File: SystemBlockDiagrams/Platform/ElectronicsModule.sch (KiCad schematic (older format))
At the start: 3 parts

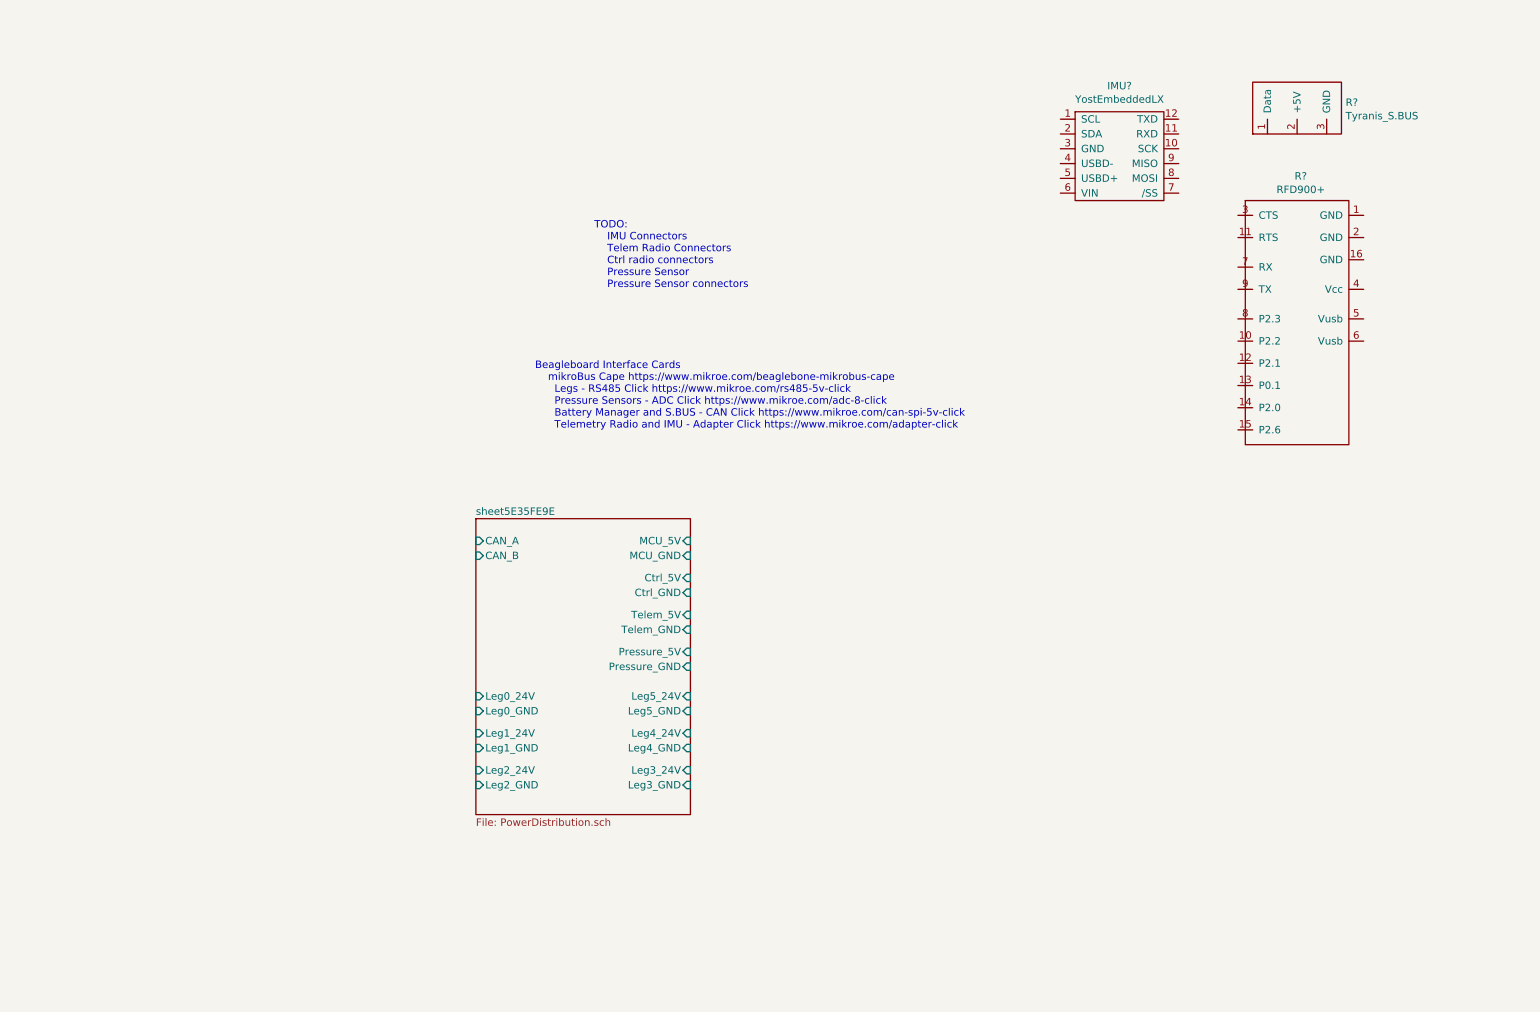
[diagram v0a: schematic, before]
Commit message: Update part numbers for BOM generation
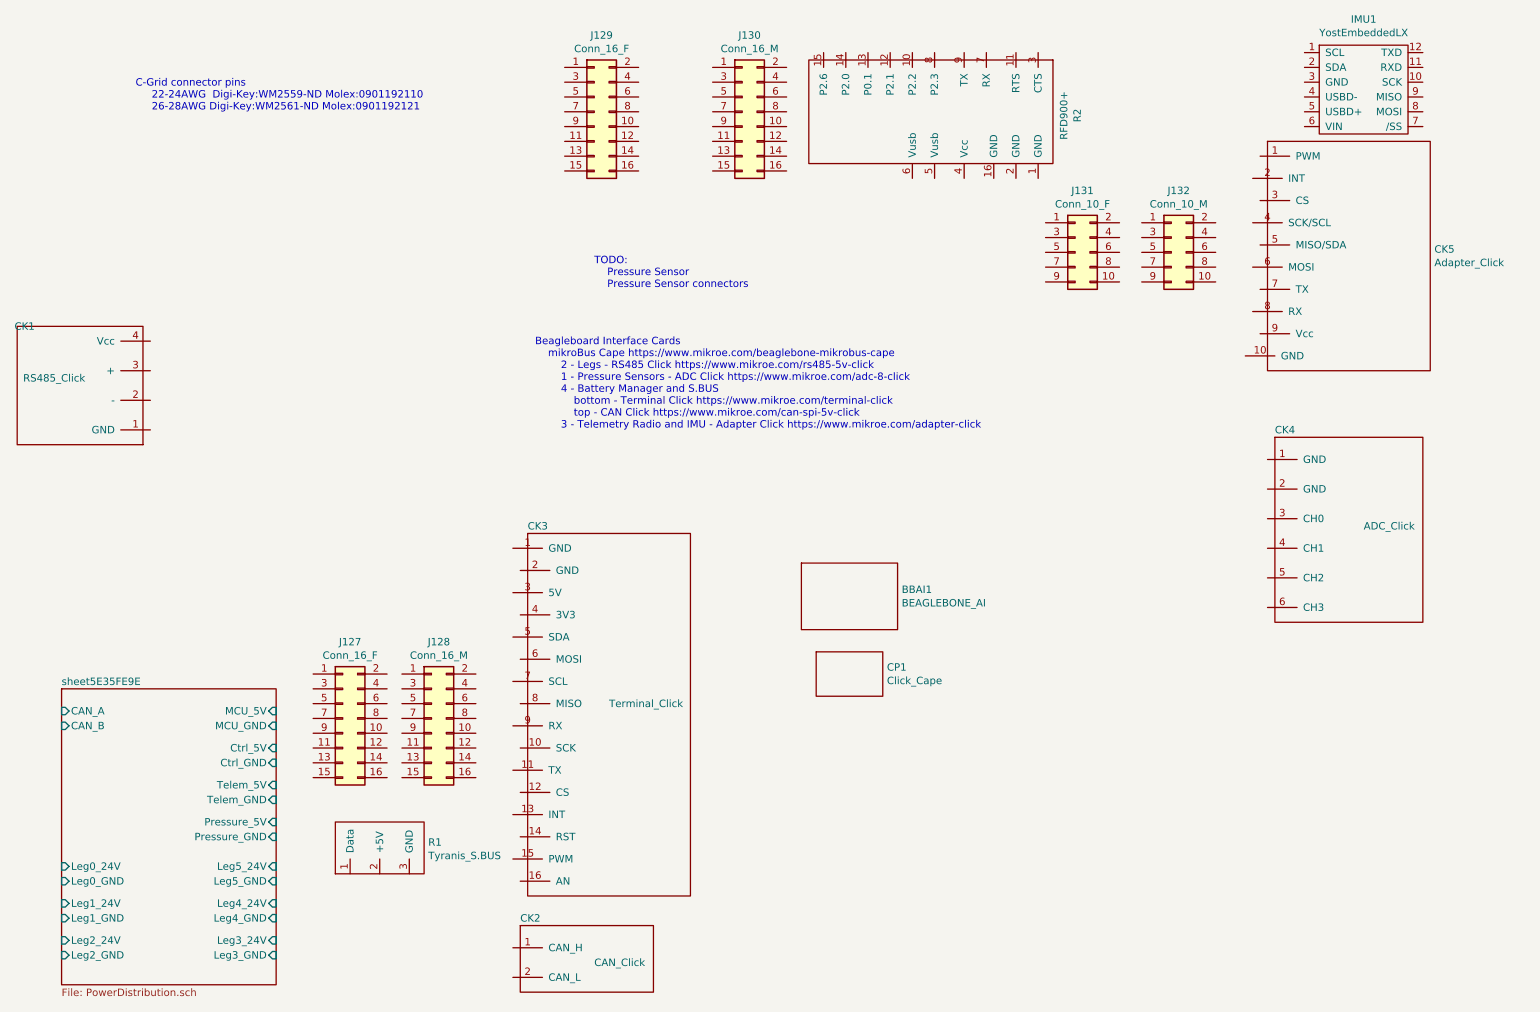
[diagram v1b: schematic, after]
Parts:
- added BBAI1: BEAGLEBONE_AI, symbol Stomp:BEAGLEBONE_AI
- added CK1: RS485_Click, symbol Stomp:RS485_Click
- added CK2: CAN_Click, symbol Stomp:CAN_Click
- added CK3: Terminal_Click, symbol Stomp:Terminal_Click
- added CK4: ADC_Click, symbol Stomp:ADC_Click
- added CK5: Adapter_Click, symbol Stomp:Adapter_Click
- added CP1: Click_Cape, symbol Stomp:Click_Cape
- added J127, J129: Conn_16_F, symbol Connector_Generic:Conn_02x08_Odd_Even
- added J128, J130: Conn_16_M, symbol Connector_Generic:Conn_02x08_Odd_Even
- added J131: Conn_10_F, symbol Connector_Generic:Conn_02x05_Odd_Even
- added J132: Conn_10_M, symbol Connector_Generic:Conn_02x05_Odd_Even
- gave numbers to parts that had none: 3
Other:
- note added: "Beagleboard Interface Cards\n mikroBus Cape https://www.mikroe.com/beaglebone-mikrobus-cape\n 2 - Legs - RS485 Click https://www.mikroe.com/rs485-5v-click\n 1 - Pressure Sensors - ADC Click https://www.mikroe.com/adc-8-click\n 4 - Battery Manager and S.BUS\n bottom - Terminal Click https://www.mikroe.com/terminal-click\n top - CAN Click https://www.mikroe.com/can-spi-5v-click\n 3 - Telemetry Radi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"
- note added: "C-Grid connector pins\n 22-24AWG Digi-Key:WM2559-ND Molex:0901192110\n 26-28AWG Digi-Key:WM2561-ND Molex:0901192121"
- note added: "TODO:\n Pressure Sensor\n Pressure Sensor connectors\n"
- note removed: "Beagleboard Interface Cards\n mikroBus Cape https://www.mikroe.com/beaglebone-mikrobus-cape\n Legs - RS485 Click https://www.mikroe.com/rs485-5v-click\n Pressure Sensors - ADC Click https://www.mikroe.com/adc-8-click\n Battery Manager and S.BUS - CAN Click https://www.mikroe.com/can-spi-5v-click\n Telemetry Radio and IMU - Adapter Click https://www.mikroe.com/adapter-click"
- note removed: "TODO:\n IMU Connectors\n Telem Radio Connectors\n Ctrl radio connectors\n Pressure Sensor\n Pressure Sensor connectors\n"
- moved on the sheet: IMU1, R1, R2
